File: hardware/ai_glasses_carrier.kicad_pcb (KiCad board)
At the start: 6 copper layers, 70 x 55 mm, 106 parts, among them J1 DF40C-100DS-0.4V(51), J2 FH35C-31S-0.3SHW(50), J3 JST-SH 2p (spkr), J31 DF40C-100DS-0.4V(51), J32 DF40C-100DS-0.4V(51), J4 GCT USB4085 (USB2), J5 JST-PH 3p, J6 JST-SH 2p, J7 Header 1x4 2.54mm, J8 U.FL / IPEX, SW1 Tact SW SMD, SW2 Tact SW SMD, SW3 Tact SW SMD, U10 ICM-42688-P, U11 DRV2605L, U12 TLV75733 (LDO), U13 TLV75718 (LDO), U14 MAX-M10S-00B-01, U15 TPS25940 (e-fuse, opt), U16 TPD4E05U06, U2 TPD4E05U06, U3 LP5907-3.3 (low-noise LDO), U4 MAX98357AETE+T, U5 TPD2E009, U6 TPS61022 (Boost), U7 BQ25180, U8 BQ29700, U9 MAX17048

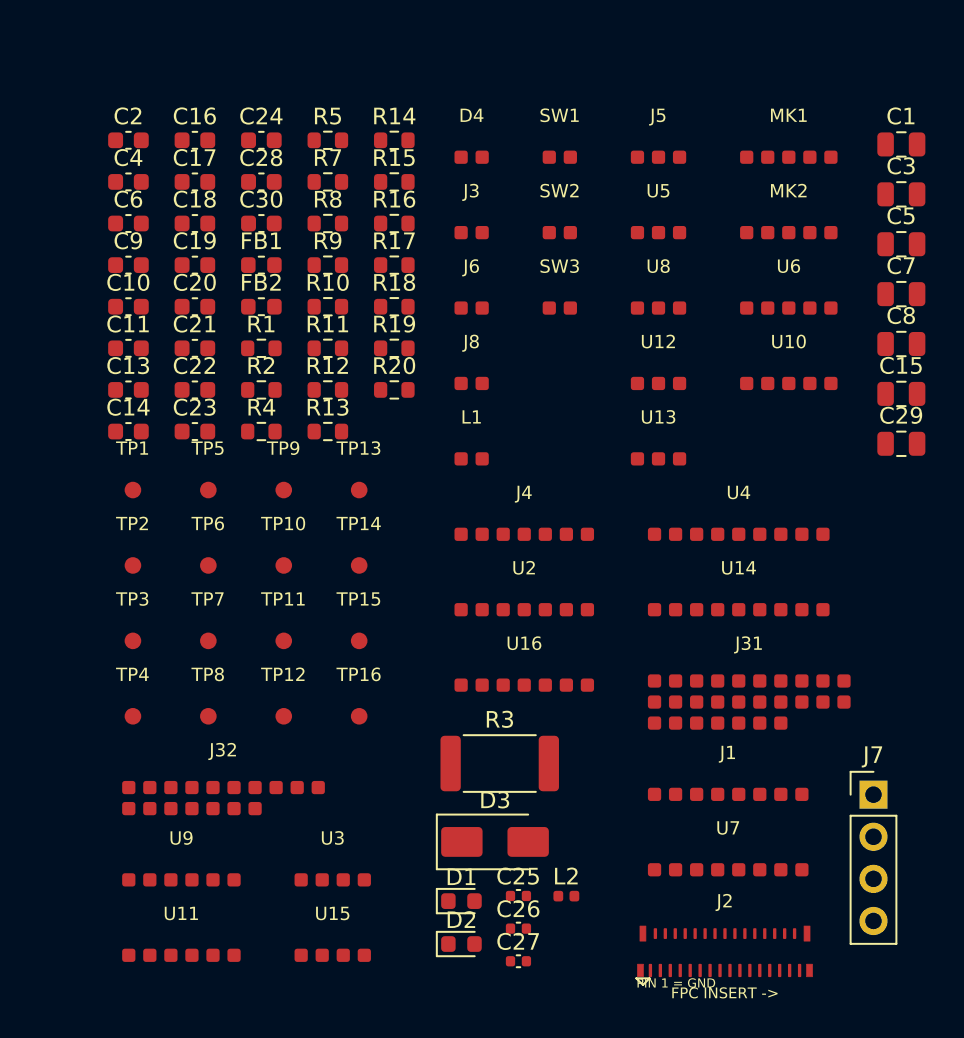
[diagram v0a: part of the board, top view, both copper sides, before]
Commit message: Update V2 chipdown schematic and mechanical package
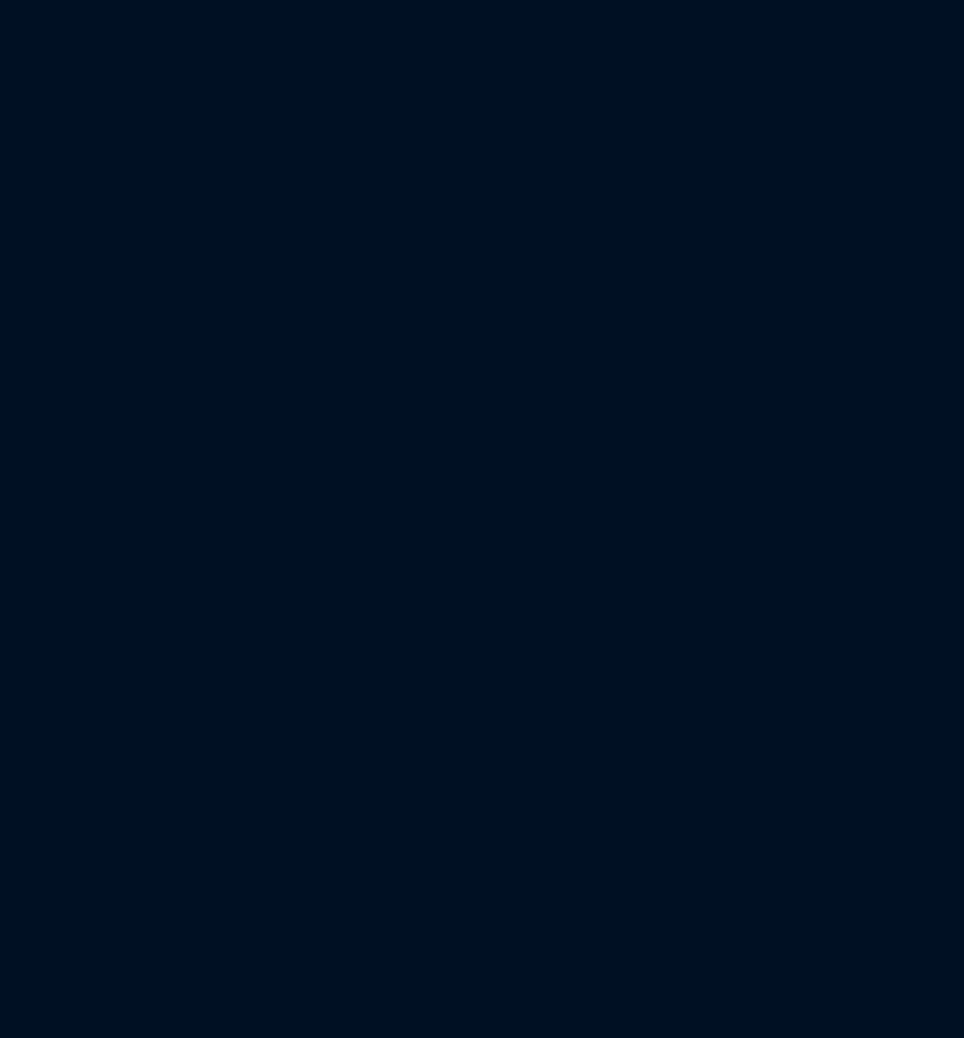
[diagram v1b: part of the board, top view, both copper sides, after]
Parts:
- removed C1, C15, C29, C3, C5, C8: 10µF, Capacitor_SMD:C_0805_2012Metric
- removed C10, C13, C14, C16, C17, C18, C19, C2, C20, C21, C22, C30, C4, C6: 100nF, Capacitor_SMD:C_0603_1608Metric
- removed C11, C9: 1µF, Capacitor_SMD:C_0603_1608Metric
- removed C23, C24: 1nF, Capacitor_SMD:C_0603_1608Metric
- removed C25, C26: π shunt (DNP,tune), Capacitor_SMD:C_0402_1005Metric
- removed C27: DC-block (series,tune), Capacitor_SMD:C_0402_1005Metric
- removed C28: 100nF (active-ant), Capacitor_SMD:C_0603_1608Metric
- removed C7: 22µF, Capacitor_SMD:C_0805_2012Metric
- removed D1: LED Green, LED_SMD:LED_0603_1608Metric
- removed D2: LED Blue, LED_SMD:LED_0603_1608Metric
- removed D3: SMAJ5.0A (TVS), Diode_SMD:D_SMA
- removed D4: ESD low-cap RF 0.3pF, AI_Glasses:RF_ESD_2P_VERIFY
- removed FB1, FB2: Ferrite 600Ω@100MHz, Inductor_SMD:L_0603_1608Metric
- removed J1: DF40C-100DS-0.4V(51), AI_Glasses:VERIFY_B2B_J1_LOGICAL
- removed J2: FH35C-31S-0.3SHW(50), AI_Glasses:FH35C-31S-0.3SHW_50
- removed J3: JST-SH 2p (spkr), AI_Glasses:VERIFY_2P
- removed J31: DF40C-100DS-0.4V(51), AI_Glasses:VERIFY_B2B_J31_LOGICAL
- removed J32: DF40C-100DS-0.4V(51), AI_Glasses:VERIFY_B2B_J32_LOGICAL
- removed J4: GCT USB4085 (USB2), AI_Glasses:VERIFY_7P
- removed J5: JST-PH 3p, AI_Glasses:VERIFY_3P
- removed J6: JST-SH 2p, AI_Glasses:VERIFY_2P
- removed J7: Header 1x4 2.54mm, Connector_PinHeader_2.54mm:PinHeader_1x04_P2.54mm_Vertical
- removed J8: U.FL / IPEX, AI_Glasses:VERIFY_2P
- removed L1: 4.7µH, AI_Glasses:POWER_INDUCTOR_7X7_VERIFY
- removed L2: RF choke (active-ant), Inductor_SMD:L_0402_1005Metric
- removed MK1, MK2: SPH0641LU4H-1, AI_Glasses:VERIFY_5P
- removed R1, R2: 5.1k, Resistor_SMD:R_0603_1608Metric
- removed R10, R12, R13, R7, R8, R9: 2.2k, Resistor_SMD:R_0603_1608Metric
- removed R11, R14, R15, R16: 10k, Resistor_SMD:R_0603_1608Metric
- removed R17: 10Ω (active-ant), Resistor_SMD:R_0603_1608Metric
- removed R18, R19, R20: 100k, Resistor_SMD:R_0603_1608Metric
- removed R3: 0R / shunt, Resistor_SMD:R_2512_6332Metric
- removed R4, R5: 1k, Resistor_SMD:R_0603_1608Metric
- removed SW1, SW2, SW3: Tact SW SMD, AI_Glasses:VERIFY_2P
- removed TP1, TP10, TP11, TP12, TP13, TP14, TP15, TP16, TP2, TP3, TP4, TP5, TP6, TP7, TP8, TP9: TestPoint 1.0mm, AI_Glasses:VERIFY_TP_1P
- removed U10: ICM-42688-P, AI_Glasses:VERIFY_5P
- removed U11: DRV2605L, AI_Glasses:VERIFY_6P
- removed U12: TLV75733 (LDO), AI_Glasses:VERIFY_3P
- removed U13: TLV75718 (LDO), AI_Glasses:VERIFY_3P
- removed U14: MAX-M10S-00B-01, AI_Glasses:VERIFY_9P
- removed U15: TPS25940 (e-fuse, opt), AI_Glasses:VERIFY_4P
- removed U16, U2: TPD4E05U06, AI_Glasses:TPD4E05U06_VERIFY
- removed U3: LP5907-3.3 (low-noise LDO), AI_Glasses:VERIFY_4P
- removed U4: MAX98357AETE+T, AI_Glasses:VERIFY_9P
- removed U5: TPD2E009, AI_Glasses:TPD2E009_VERIFY
- removed U6: TPS61022 (Boost), AI_Glasses:VERIFY_5P
- removed U7: BQ25180, AI_Glasses:VERIFY_8P
- removed U8: BQ29700, AI_Glasses:VERIFY_3P
- removed U9: MAX17048, AI_Glasses:VERIFY_6P
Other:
- rule pad_to_mask_clearance: 0.05 -> 0.050
